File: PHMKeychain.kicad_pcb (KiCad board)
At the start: 2 copper layers, 31.2 x 40 mm, 12 parts, among them J1 Conn_02x03_Odd_Even, Q1 HL2301A, U1 ATTINY85-20SU_C31540447

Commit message: Organized
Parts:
- J1: value Conn_02x03_Odd_Even -> Conn_01x06; footprint Connector_PinHeader_1.00mm:PinHeader_1x06_P1.00mm_Vertical -> Connector_PinHeader_2.54mm:PinHeader_1x06_P2.54mm_Vertical
- moved C2 63.9 mm to (86.4, 108.6), turned to 90 degrees
- moved C1 62.7 mm to (86.2, 106.0), turned to 90 degrees
- moved C3 62.2 mm to (89.8, 113.4), turned to 0 degrees
- moved R2 62.0 mm to (89.2, 116.6), turned to 0 degrees
- moved U1 58.8 mm to (89.8, 107.4), turned to 0 degrees
- moved D1 56.8 mm to (94.0, 113.2), turned to 90 degrees
- moved R1 53.4 mm to (91.8, 100.4)
- moved Q1 51.6 mm to (88.4, 100.0)
- moved S1 49.4 mm to (100.2, 116.4), turned to 90 degrees
- moved BT1 49.4 mm to (100.0, 88.0)
- moved LS1 46.0 mm to (100.0, 104.0)
- moved J1 37.3 mm to (112.4, 104.7), turned to 0 degrees
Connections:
- net MOSI / LATCH renamed LATCH
- C3 pad 1: Net-(LS1-LEAD+) -> Net-(U1-PB4)
- C3 pad 2: Net-(U1-PB4) -> Net-(LS1-LEAD+)
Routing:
- net Net-(LS1-LEAD+): track 3.90 -> 27.1 mm, vias 0 -> 2
- net LATCH: track 58.8 -> 40.1 mm, vias 1 -> 0
- net VBAT: track 55.7 -> 44.8 mm
- net MISO: track 31.1 -> 22.7 mm
- net Net-(D1-Pad2): track 1.82 -> 7.51 mm
- net GND: track 19.3 -> 14.4 mm, vias 6 -> 7
- net RESET: track 27.9 -> 30.8 mm, vias 0 -> 1
- net SCK: track 26.7 -> 25.7 mm
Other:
- board size 31.2 x 40 mm -> 30 x 40 mm

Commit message: Clean up board
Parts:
- S1: value Tactile Button, 160gf -> Tactile Button
- moved R2 29.2 mm to (110.3, 96.4), turned to 90 degrees
- moved D1 25.0 mm to (112.4, 96.3)
- moved J1 3.61 mm to (112.4, 101.0)
- moved S1 2.80 mm to (100.2, 113.6), turned to 180 degrees
- moved R1 1.85 mm to (91.8, 98.5)
- moved Q1 1.85 mm to (88.4, 98.2)
- moved C3 1.65 mm to (91.4, 113.8)
- moved C2 0.20 mm to (86.2, 108.6)
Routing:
- net Net-(LS1-LEAD+): track 27.1 -> 20.4 mm, vias 2 -> 0
- net VBAT: track 44.8 -> 38.2 mm
- net Net-(D1-Pad2): track 7.51 -> 2.55 mm
- net RESET: track 30.8 -> 26.7 mm
- net LATCH: track 40.1 -> 43.1 mm, vias 0 -> 1
- net MISO: track 22.7 -> 25.2 mm
- net GND: track 14.4 -> 15.6 mm
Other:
- board size 30 x 40 mm -> 30 x 36 mm

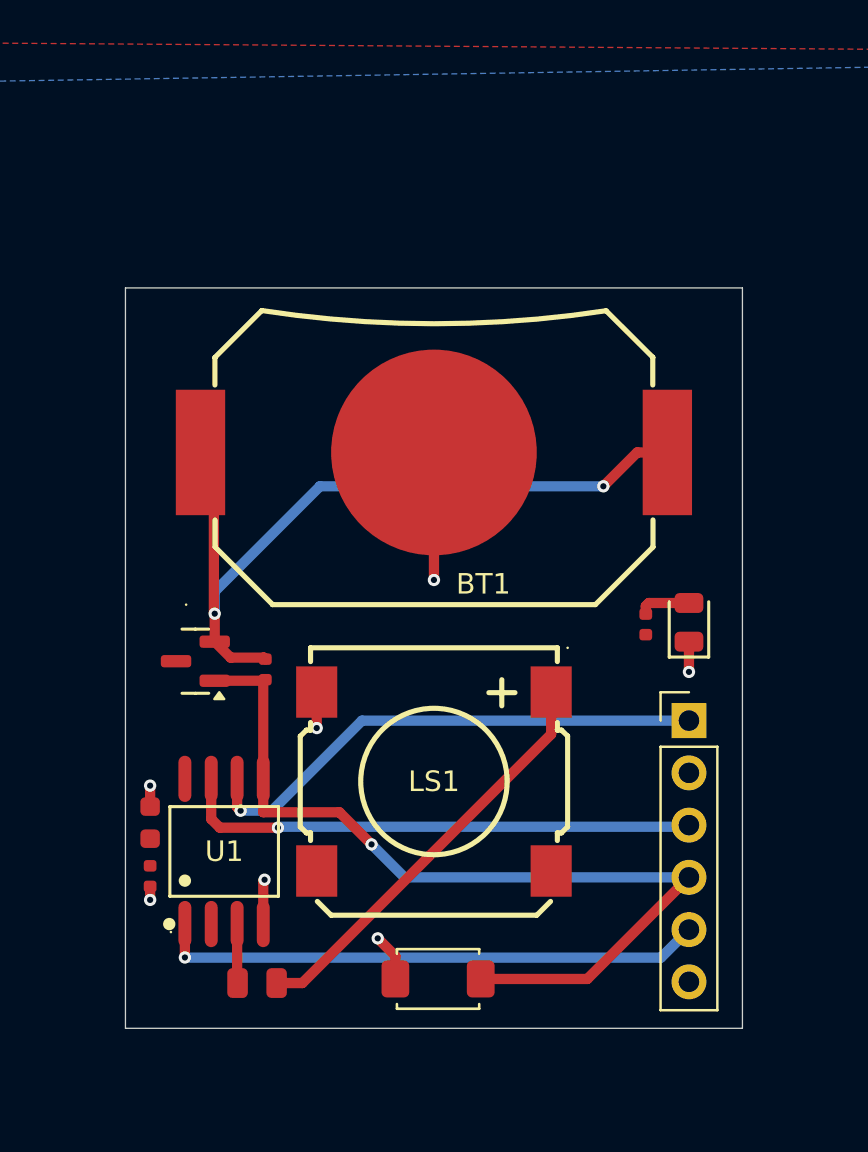
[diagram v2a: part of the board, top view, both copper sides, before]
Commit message: Added Art
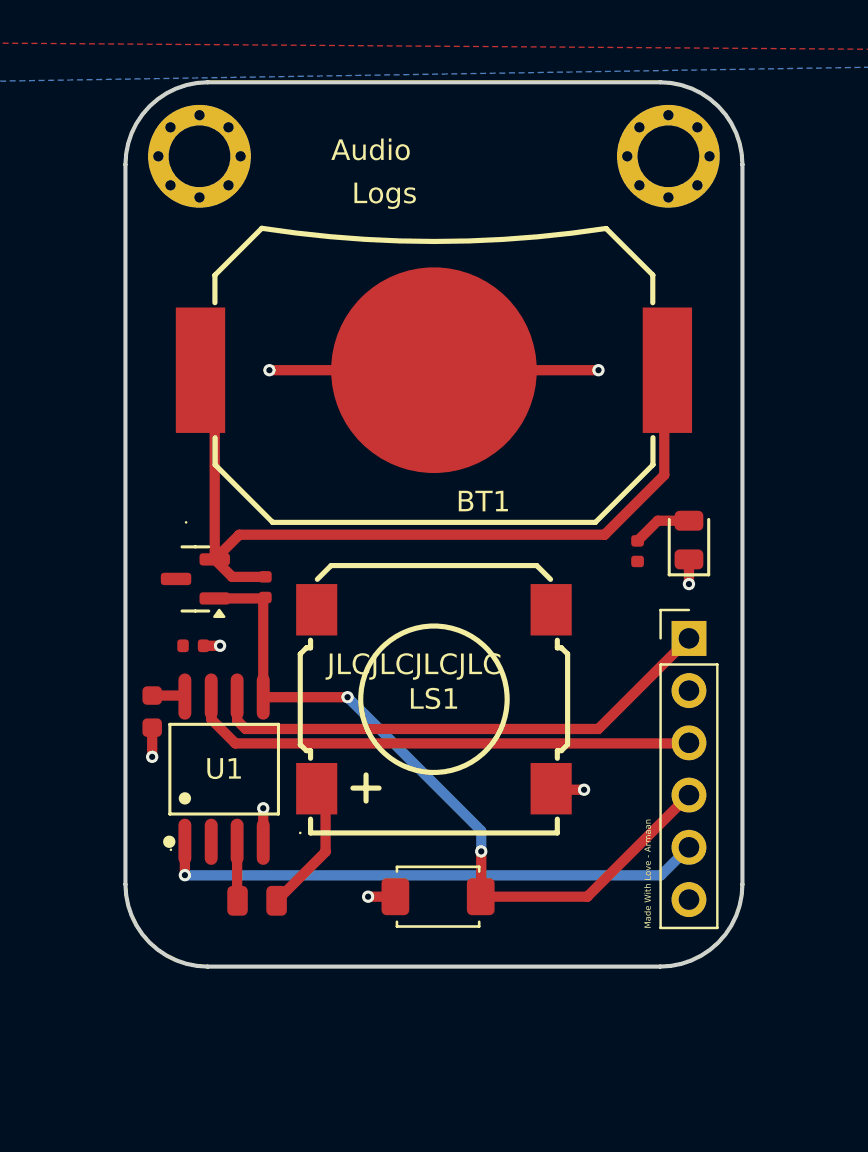
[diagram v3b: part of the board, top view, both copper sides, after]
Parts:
- added G*** (x2): LOGO, LOGO, B.Cu at (90.7, 107.3)
- added G***: LOGO, LOGO, B.Cu at (91.4, 97.3)
- added H1: ~, PCM_JLCPCB:Hole, 3mm, F.Cu at (111.4, 73.6)
- added H2: ~, PCM_JLCPCB:Hole, 3mm, F.Cu at (88.6, 73.6)
- moved C2 11.4 mm to (88.3, 97.4), turned to 180 degrees
- moved C1 5.40 mm to (86.3, 100.6), turned to -90 degrees
- moved BT1 4.00 mm to (100.0, 84.0)
- moved C3 4.00 mm to (91.4, 109.8)
- moved D1 4.00 mm to (112.4, 92.3)
- moved J1 4.00 mm to (112.4, 97.0)
- moved LS1 4.00 mm to (100.0, 100.0), turned to 0 degrees
- moved Q1 4.00 mm to (88.4, 94.2)
- moved R1 4.00 mm to (91.8, 94.5)
- moved S1 4.00 mm to (100.2, 109.6)
- moved U1 4.00 mm to (89.8, 103.4)
- moved R2 3.58 mm to (109.9, 92.8)
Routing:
- net Net-(LS1-LEAD+): track 20.4 -> 6.76 mm
- net GND: track 15.6 -> 25.6 mm, vias 7 -> 8
- net LATCH: track 43.1 -> 36.0 mm, vias 1 -> 2
- net VBAT: track 38.2 -> 41.9 mm, vias 2 -> 0
- net VCC: track 0.00 -> 1.61 mm
- net SCK: track 25.4 -> 25.1 mm, vias 1 -> 0
- net MISO: track 25.2 -> 25.1 mm, vias 1 -> 0
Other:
- board size 30 x 36 mm -> 30 x 43 mm
- board text added: "Alyssa"
- board text added: "Antonia"
- board text added: "Armaan"
- board text added: "Audio"
- board text added: "Crew:"
- board text added: "HAIL MARY"
- board text added: "JLCJLCJLCJLC"
- board text added: "Kellie"
- board text added: "Logs"
- board text added: "Made With Love - Armaan"
- board text added: "Mission Date: March 24, 2026"
- board text added: "Project"
